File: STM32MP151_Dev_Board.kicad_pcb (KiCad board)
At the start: 2 copper layers, 72 x 106 mm, 79 parts, among them J1 MY-TFT070CV2, J11 CTP, J12 USB_DEBUG, J13 USB_2, J2 AudioJack3, J3 SWDIO, J4 UART4, J5 BOOT_SD, J8 USB_1, J9 AFY480272A0, SW1 BOOT, SW2 RESET, U1 MYC-YA151C-256N256D, U2 FT231XS, U3 TPS2042D, U4 PCM3060PWR, U5 TPD2EUSB30, U6 R1218NO41, U7 ESP8285, Y2 26MHz

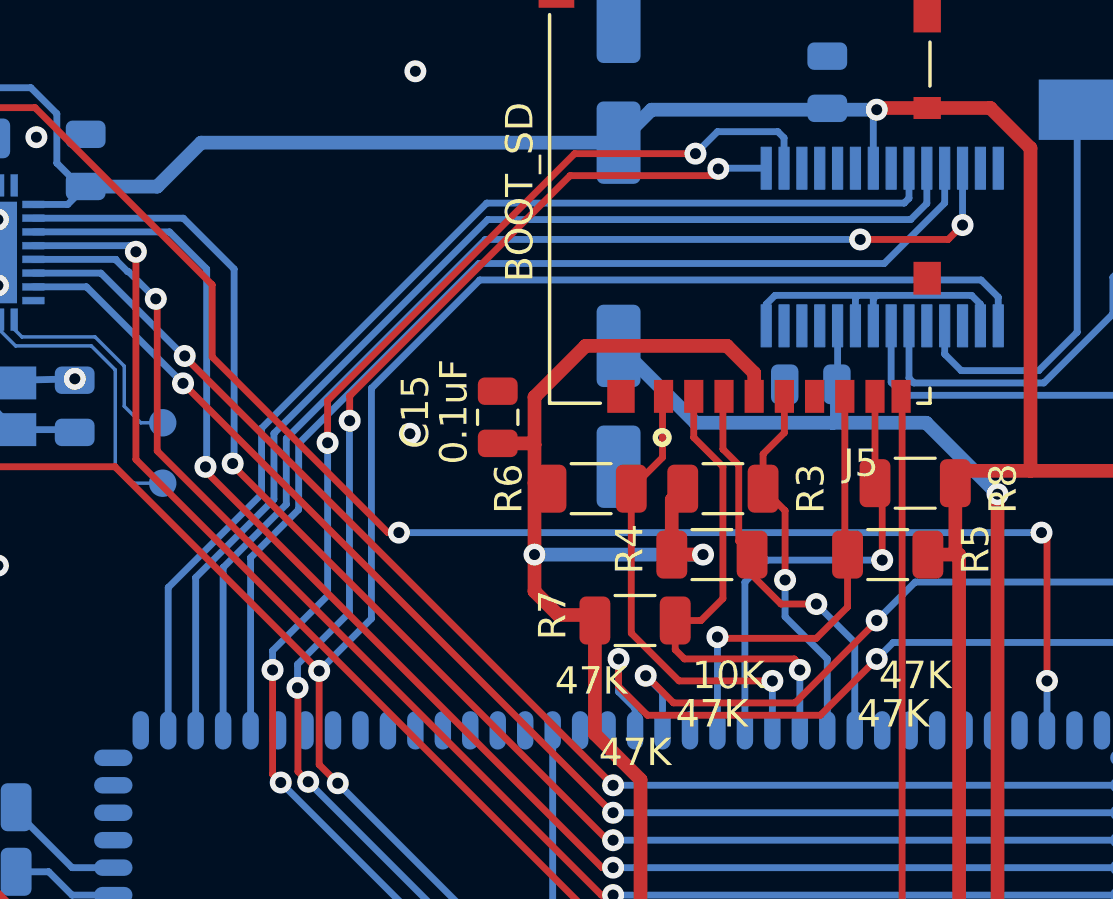
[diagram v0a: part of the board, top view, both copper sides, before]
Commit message: swap SAI clock signals. UPdate rev numbmer
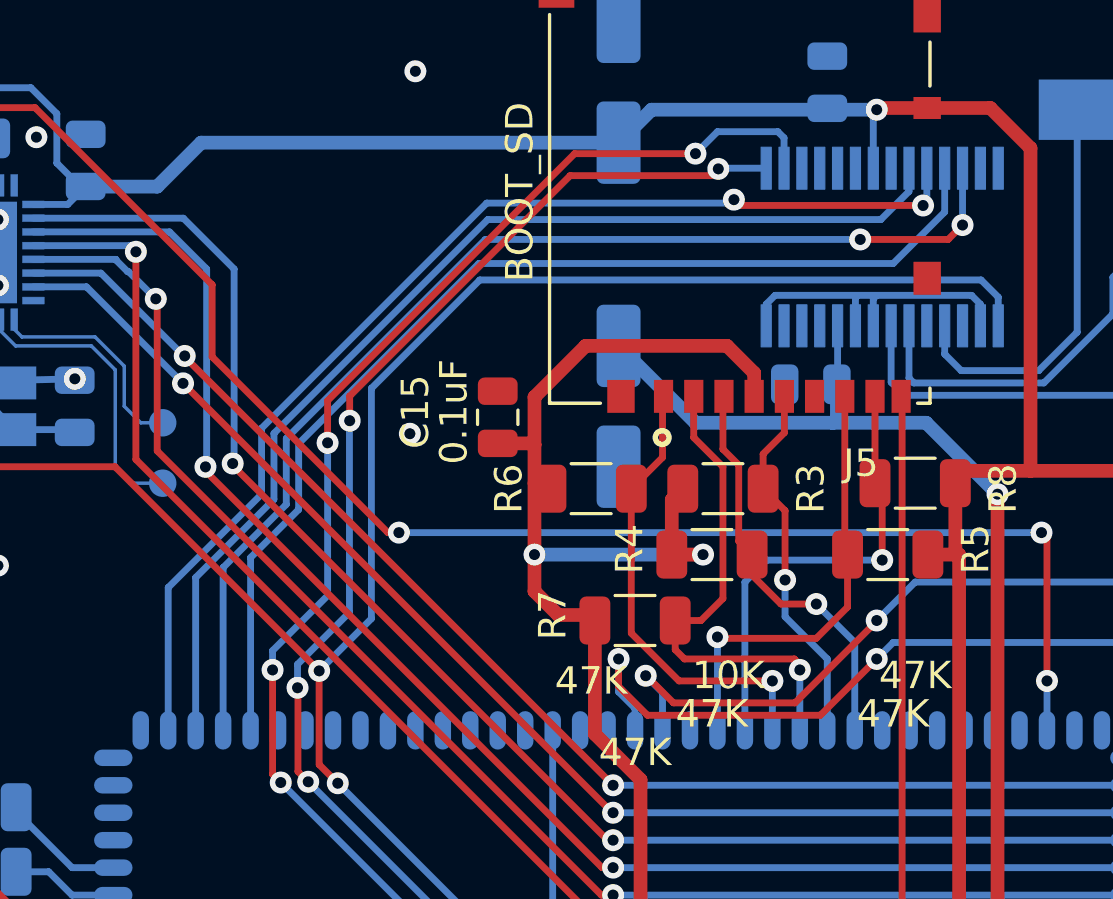
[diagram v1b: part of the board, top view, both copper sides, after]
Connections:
- U4 pad 10: SAI1_MCLK_B -> SAI1_SCK_B
- U4 pad 9: SAI1_SCK_B -> SAI1_MCLK_B
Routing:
- net SAI1_MCLK_B: track 40.5 -> 39.6 mm
- net SAI1_SCK_B: track 40.5 -> 41.4 mm, vias 0 -> 2
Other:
- board text added: "REV C"
- board text removed: "REV B"
